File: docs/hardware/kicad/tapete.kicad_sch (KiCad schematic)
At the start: 32 parts, among them U1 ESP32-DevKit-30, U2 ULN2803A, U3 DFPlayer-Mini

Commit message: feat(figuras): planos KiCad, diagrama de bloques y simulacion SPICE en el articulo
El articulo solo tenia figuras de simulacion de la logica y dos fotos. Ahora
incorpora la ingenieria electrica, con la misma regla: ninguna figura se dibuja a
mano y ninguna puede divergir del codigo.

**KiCad.** El esquematico era un auto-layout ilegible: la sexta columna de LEDs se
salia del marco, el cajetin estaba vacio y cada etiqueta de net se dibujaba encima
de su componente. Arreglado:
- `kisch.py`: soporte de cajetin (`TitleBlock`) y etiquetas justificadas HACIA AFUERA
  del simbolo (los pines del lado izquierdo llevaban el texto sobre el cuerpo).
- `gen_tapete.py`: layout por bloques funcionales (sensado 3V3 | computo | actuacion
  5V | audio), LEDs en 2x3 como las casillas fisicas, todo dentro del marco A3.
- `scripts/gen_esquematico.py`: regenera, corre ERC (**aborta si hay infracciones**),
  exporta PDF/SVG y produce el PNG rotado del Anexo A.
- **El netlist NO cambio**: 47 nets identicas nodo a nodo antes y despues. El cambio
  es puramente grafico. Verificado ademas por circuit-reviewer: los mapas de pines
  reproducen exactamente `Config.h` (FSR 36,39,34,35,32,33 / LED 4,5,18,19,21,23),
  DFPlayer cruzado con 1k en serie, sin puente 3V3<->5V, los 6 FSR en ADC1.
- Corregida una cita cruzada muerta impresa en el plano (cableado.md 4.4 -> Paso 7).

**Diagrama de bloques** (`scripts/gen_diagrama_bloques.py`, graphviz): arquitectura con
los dos dominios de alimentacion separados. Los GPIO se leen de `Config.h`.

**SPICE (evidencia E9 nueva).** `simulator/spice.py` corre ngspice sobre los netlists
de `docs/hardware/spice/` y contrasta el divisor del FSR con su solucion cerrada:
error maximo 2,9e-06 V sobre 11 puntos. Resultado util: el umbral de 2000 cuentas
equivale a 1,61 V y exige que el FSR baje a **10,5 kOhm** — acota la calibracion
pendiente sin tocar el prototipo. La corriente del grupo LED (192 uA/LED) se reporta
como ESTIMACION: su modelo de diodo y V_CE(sat) son as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
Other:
- note added: "Alimentacion: USB del PC -> VIN(5V) del ESP32. Los rieles 3V3 y 5V NUNCA se puentean. Conectividad definida por etiquetas de net (label): mismo nombre = mismo nodo."
- note added: "BLOQUE 1 - SENSADO (3V3): 6 canales 3V3 -[FSR]- nodo -[10k]- GND ; nodo -> ADC1"
- note added: "BLOQUE 3 - ACTUACION (5V): 5V -[2k2]- anodo LED ; catodo -> OUTk del ULN2803A"
- note added: "BLOQUE 4 - AUDIO (5V): UART2 del ESP32 -[1k]-> RX del DFPlayer ; TX -> RX2. Contingencia GPIO16 (cableado.md, Paso 7): GPIO16 no es 5V-tolerante. Si el TX del DFPlayer mide ~5 V, intercalar divisor 1k+2k en DF_TX. Nominal (3,3 V) = directo."
- note removed: "Contingencia GPIO16 (cableado.md 4.4): si DFPlayer TX mide ~5V, intercalar divisor 1k+2k en DF_TX. Nominal (3.3V) = directo."
- note removed: "Tapete Interactivo - esquematico (auto-layout; reordenar en GUI). Fuente: docs/hardware/cableado.md + Config.h"
- company: (none) -> Universidad Santiago de Cali - Ingenieria Electronica
- title: (none) -> Tapete Interactivo Terapeutico - Esquematico del sistema
- moved on the sheet: C1, C2, C3, D1, D2, D3, D4, D5, D6, LS1, R1, R10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

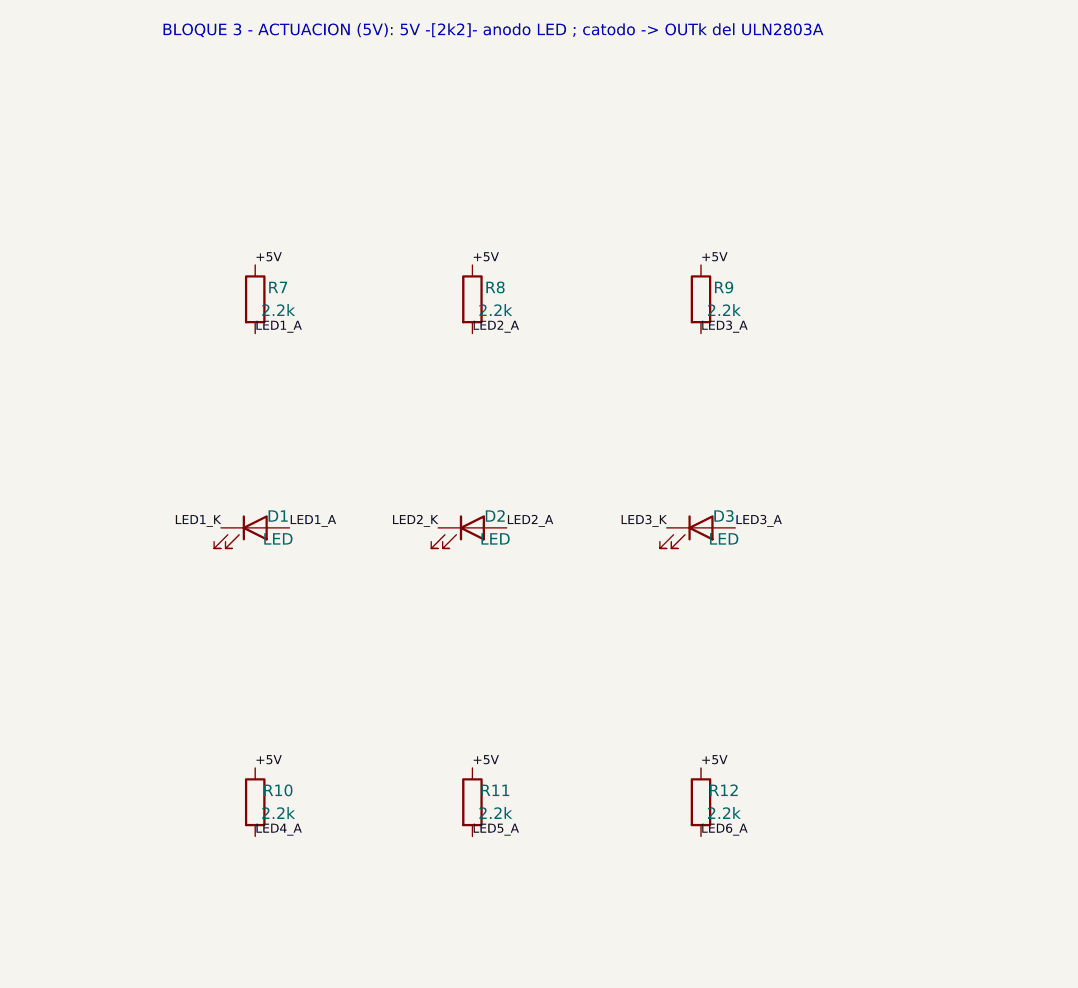
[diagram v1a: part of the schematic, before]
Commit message: fix(hardware): LEDs a 110 ohm — sincronizar TODAS las fuentes con el tapete real
El autor cambio las 6 resistencias de grupo de 2.2 kOhm a 110 Ohm porque el brillo
era demasiado tenue, y verifico en hardware los 3 modos x 3 niveles con los tonos
nuevos: todo funciona, sin brownout (incluido Equilibrio n3, el peor caso: 4 grupos
encendidos + audio).

Medido con ngspice (instrumento del proyecto), no a mano:
- antes: 0,58 mA por grupo / 0,19 mA por LED  -> tenue
- ahora: 10,1 mA por grupo / 3,4 mA por LED   -> ~61 mA los 6 grupos

Sigue un orden de magnitud por debajo del ULN2803A (500 mA/canal de maximo absoluto,
uln2803a.pdf). El maximo del LED es DESCONOCIDO: no hay datasheet del LED en el repo.

Sincronizadas TODAS las fuentes que decian 2.2 kOhm y ya no describian el hardware:
cableado.md, 00_diseno_circuito.md, materiales.md, spice/grupo_led.cir, el generador
del esquematico (gen_tapete.py -> tapete.kicad_sch/pdf/cir/bom + esquematico.png del
articulo), resultados.json y el articulo (3 puntos + los conteos de la suite).
El esquematico se regenero con ERC sin infracciones y se verifico que la CONECTIVIDAD
es identica nodo a nodo: lo unico que cambia es el valor de R7..R12.

Tests: el de spice codificaba el diseno viejo ("< 1 mA por LED = tenue"). Reescrito
contra el limite CITABLE (el del ULN, que si tiene datasheet) + un test que falla si
alguien vuelve a subir la R y devuelve los LEDs a la penumbra.

Leccion (a CLAUDE.md y cableado.md): el DFPlayer mudo casi nunca es una averia, esta
COLGADO. Cambiar las resistencias con el USB conectado lo colgo: no revivio con EN ni
reseteando el ESP32, solo desconectando y reconectando la alimentacion.

Suite: 58 casos / 2186 aserciones C++ + 145 pytest, verde.

Co-Authored-By: Claude Opus 4.8 (1M context) <noreply@anthropic.com>
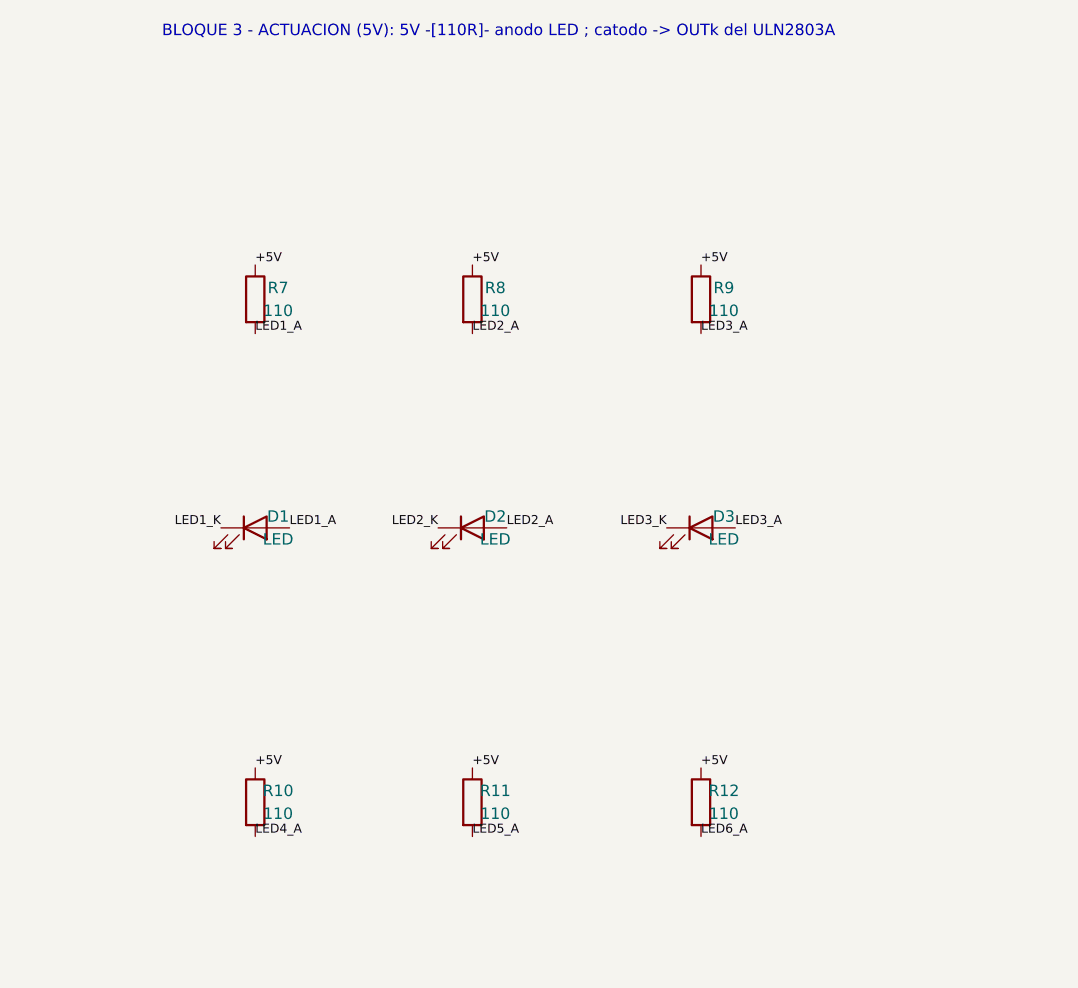
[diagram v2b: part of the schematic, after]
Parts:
- R10, R11, R12, R7, R8, R9: value 2.2k -> 110
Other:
- note added: "BLOQUE 3 - ACTUACION (5V): 5V -[110R]- anodo LED ; catodo -> OUTk del ULN2803A"
- note removed: "BLOQUE 3 - ACTUACION (5V): 5V -[2k2]- anodo LED ; catodo -> OUTk del ULN2803A"
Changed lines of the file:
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@@
 			)
 		)
-		(property "Value" "2.2k"
+		(property "Value" "110"
 			(at 342.9 60.96 0)
 			(effects
@@
 			)
 		)
-		(property "Value" "2.2k"
+		(property "Value" "110"
 			(at 367.03 60.96 0)
 			(effects
@@
 			)
 		)
-		(property "Value" "2.2k"
+		(property "Value" "110"
 			(at 392.43 60.96 0)
 			(effects
@@
 			)
 		)
-		(property "Value" "2.2k"
+		(property "Value" "110"
 			(at 342.9 116.84 0)
 			(effects
@@
 			)
 		)
-		(property "Value" "2.2k"
+		(property "Value" "110"
 			(at 367.03 116.84 0)
 			(effects
@@
 			)
 		)
-		(property "Value" "2.2k"
+		(property "Value" "110"
 			(at 392.43 116.84 0)
 			(effects
@@
 		)
 	)
-	(text "BLOQUE 3 - ACTUACION (5V): 5V -[2k2]- anodo LED ; catodo -> OUTk del ULN2803A"
+	(text "BLOQUE 3 - ACTUACION (5V): 5V -[110R]- anodo LED ; catodo -> OUTk del ULN2803A"
 		(at 330 30 0)
 		(effects
